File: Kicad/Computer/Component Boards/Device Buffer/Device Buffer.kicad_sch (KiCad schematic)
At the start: 18 parts, among them IC1 SN74ABT245BDBR, IC2 SN74ABT245BDBR, IC3 SN74ABT245BDBR, IC4 SN74ABT245BDBR, IC5 AP7365-33WG-7, J2 Conn_02x32_Counter_Clockwise

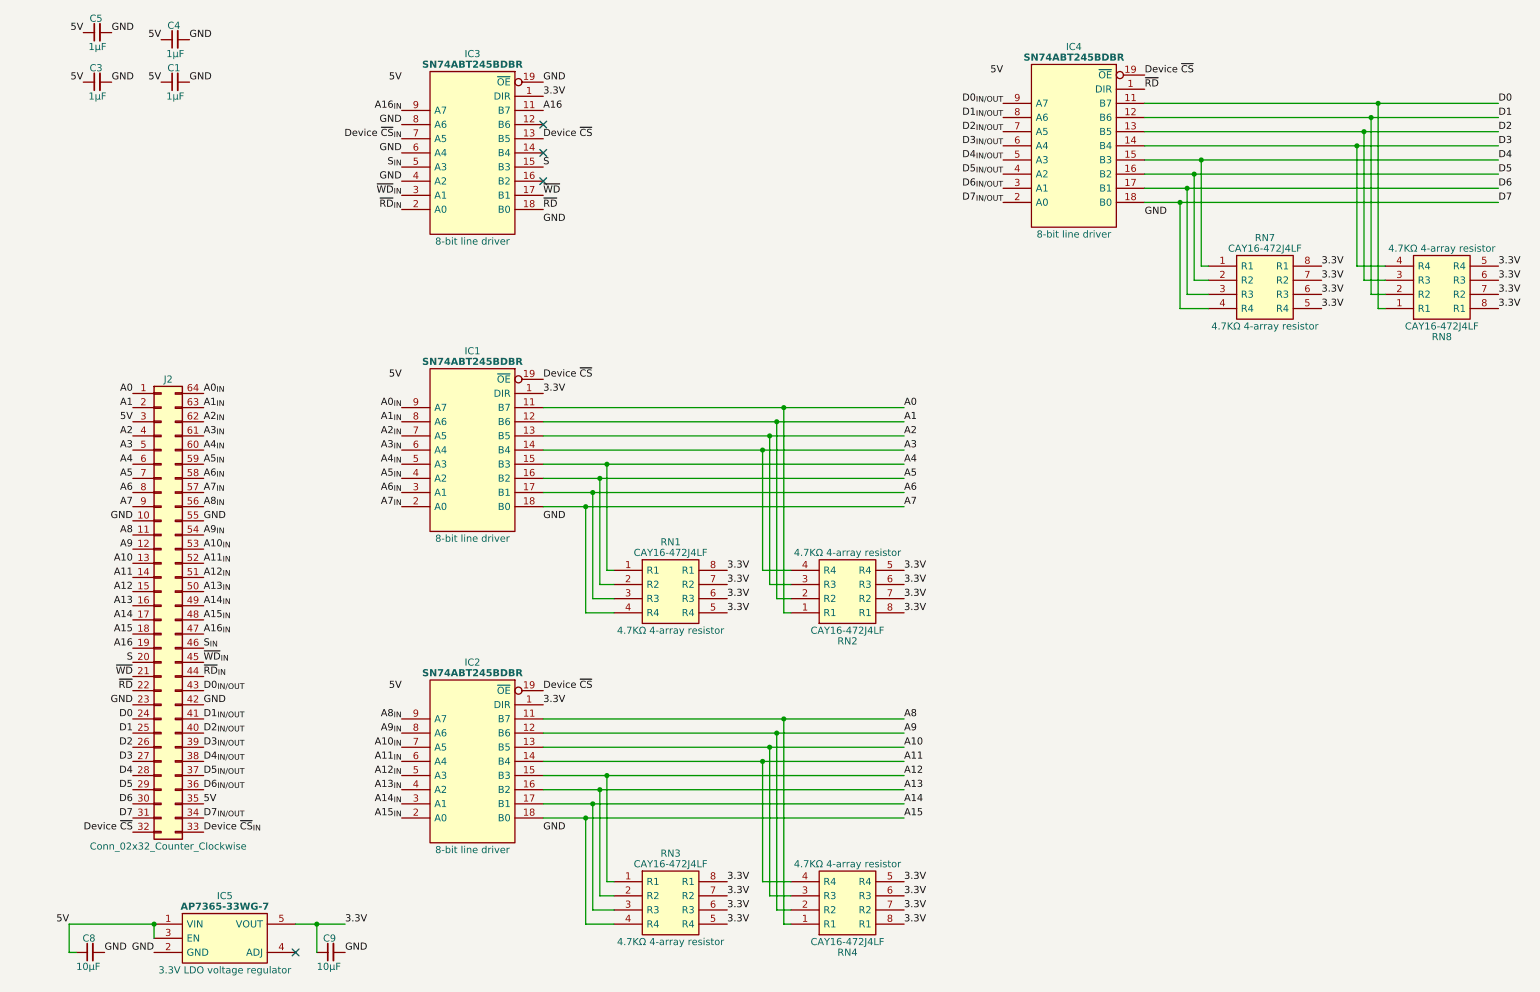
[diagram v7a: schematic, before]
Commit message: Swapped Device Buffer pin sides and re-routed.
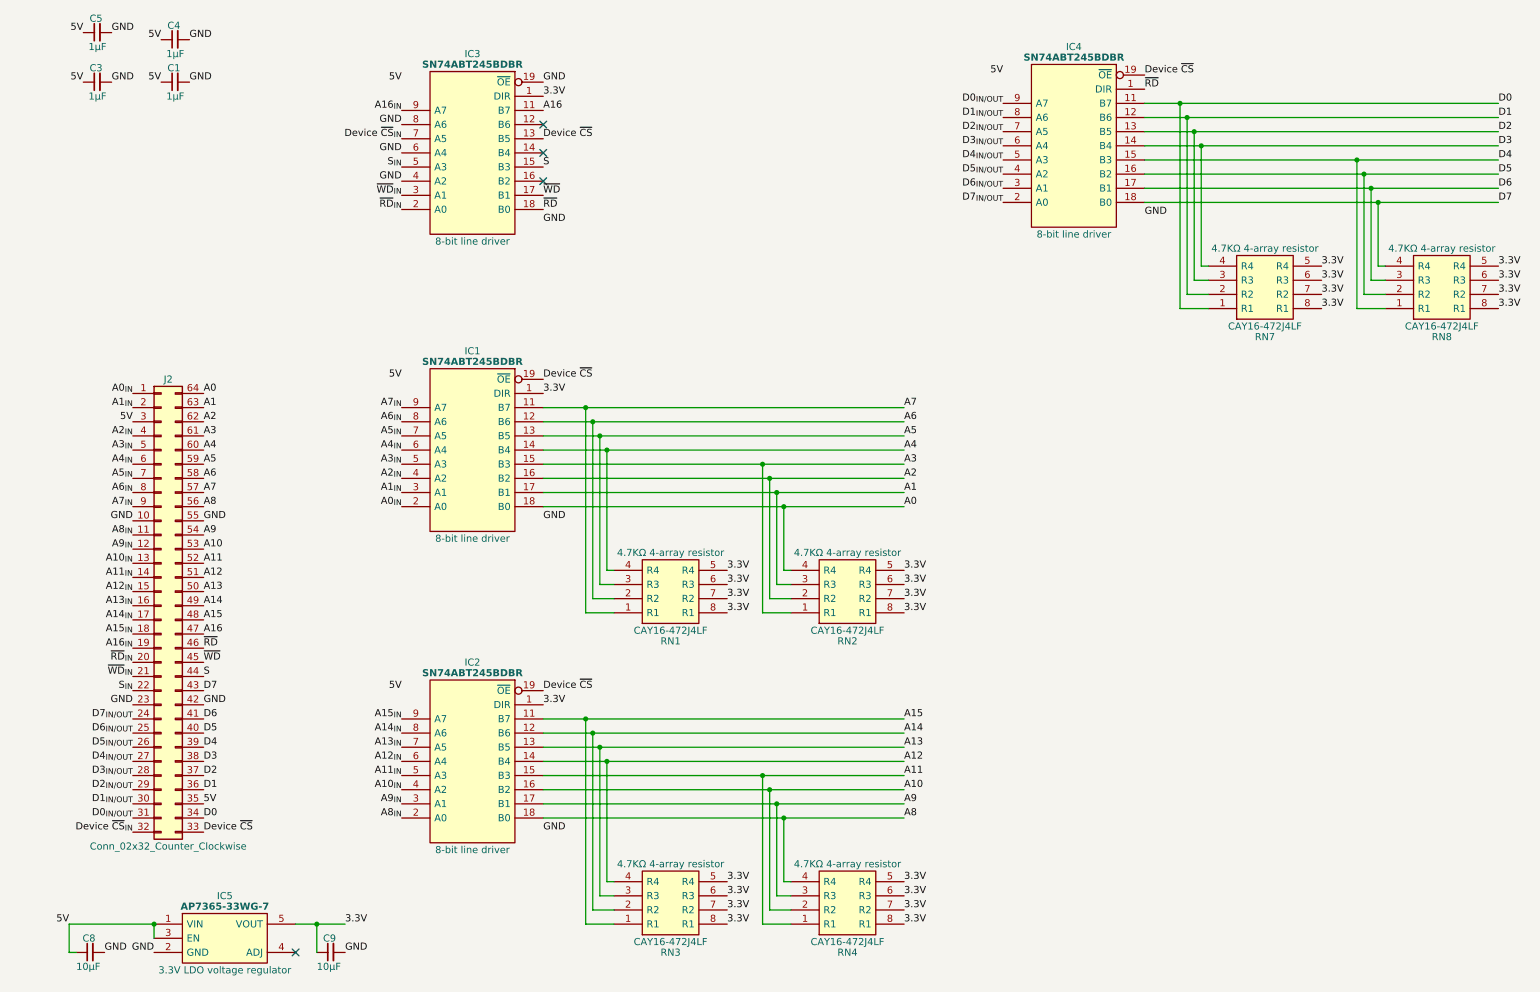
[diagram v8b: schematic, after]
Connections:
- net A0: now also IC1.18 (B0), J2.64 (Pin_64), RN2.4 (R4); no longer IC1.11 (B7), J2.1 (Pin_1), RN2.1 (R1)
- net A0_{IN}: now also IC1.2 (A0), J2.1 (Pin_1); no longer IC1.9 (A7), J2.64 (Pin_64)
- net A1: now also IC1.17 (B1), J2.63 (Pin_63), RN2.3 (R3); no longer IC1.12 (B6), J2.2 (Pin_2), RN2.2 (R2)
- net A10: now also IC2.16 (B2), J2.53 (Pin_53), RN4.2 (R2); no longer IC2.13 (B5), J2.13 (Pin_13), RN4.3 (R3)
- net A10_{IN}: now also IC2.4 (A2), J2.13 (Pin_13); no longer IC2.7 (A5), J2.53 (Pin_53)
- net A11: now also IC2.15 (B3), J2.52 (Pin_52), RN4.1 (R1); no longer IC2.14 (B4), J2.14 (Pin_14), RN4.4 (R4)
- net A11_{IN}: now also IC2.5 (A3), J2.14 (Pin_14); no longer IC2.6 (A4), J2.52 (Pin_52)
- net A12: now also IC2.14 (B4), J2.51 (Pin_51), RN3.4 (R4); no longer IC2.15 (B3), J2.15 (Pin_15), RN3.1 (R1)
- net A12_{IN}: now also IC2.6 (A4), J2.15 (Pin_15); no longer IC2.5 (A3), J2.51 (Pin_51)
- net A13: now also IC2.13 (B5), J2.50 (Pin_50), RN3.3 (R3); no longer IC2.16 (B2), J2.16 (Pin_16), RN3.2 (R2)
- net A13_{IN}: now also IC2.7 (A5), J2.16 (Pin_16); no longer IC2.4 (A2), J2.50 (Pin_50)
- net A14: now also IC2.12 (B6), J2.49 (Pin_49), RN3.2 (R2); no longer IC2.17 (B1), J2.17 (Pin_17), RN3.3 (R3)
- net A14_{IN}: now also IC2.8 (A6), J2.17 (Pin_17); no longer IC2.3 (A1), J2.49 (Pin_49)
- net A15: now also IC2.11 (B7), J2.48 (Pin_48), RN3.1 (R1); no longer IC2.18 (B0), J2.18 (Pin_18), RN3.4 (R4)
- net A15_{IN}: now also IC2.9 (A7), J2.18 (Pin_18); no longer IC2.2 (A0), J2.48 (Pin_48)
- net A16: now also J2.47 (Pin_47); no longer J2.19 (Pin_19)
- net A16_{IN}: now also J2.19 (Pin_19); no longer J2.47 (Pin_47)
- net A1_{IN}: now also IC1.3 (A1), J2.2 (Pin_2); no longer IC1.8 (A6), J2.63 (Pin_63)
- net A2: now also IC1.16 (B2), J2.62 (Pin_62), RN2.2 (R2); no longer IC1.13 (B5), J2.4 (Pin_4), RN2.3 (R3)
- net A2_{IN}: now also IC1.4 (A2), J2.4 (Pin_4); no longer IC1.7 (A5), J2.62 (Pin_62)
- net A3: now also IC1.15 (B3), J2.61 (Pin_61), RN2.1 (R1); no longer IC1.14 (B4), J2.5 (Pin_5), RN2.4 (R4)
- net A3_{IN}: now also IC1.5 (A3), J2.5 (Pin_5); no longer IC1.6 (A4), J2.61 (Pin_61)
- net A4: now also IC1.14 (B4), J2.60 (Pin_60), RN1.4 (R4); no longer IC1.15 (B3), J2.6 (Pin_6), RN1.1 (R1)
- net A4_{IN}: now also IC1.6 (A4), J2.6 (Pin_6); no longer IC1.5 (A3), J2.60 (Pin_60)
- net A5: now also IC1.13 (B5), J2.59 (Pin_59), RN1.3 (R3); no longer IC1.16 (B2), J2.7 (Pin_7), RN1.2 (R2)
- net A5_{IN}: now also IC1.7 (A5), J2.7 (Pin_7); no longer IC1.4 (A2), J2.59 (Pin_59)
- net A6: now also IC1.12 (B6), J2.58 (Pin_58), RN1.2 (R2); no longer IC1.17 (B1), J2.8 (Pin_8), RN1.3 (R3)
- net A6_{IN}: now also IC1.8 (A6), J2.8 (Pin_8); no longer IC1.3 (A1), J2.58 (Pin_58)
- net A7: now also IC1.11 (B7), J2.57 (Pin_57), RN1.1 (R1); no longer IC1.18 (B0), J2.9 (Pin_9), RN1.4 (R4)
- net A7_{IN}: now also IC1.9 (A7), J2.9 (Pin_9); no longer IC1.2 (A0), J2.57 (Pin_57)
- net A8: now also IC2.18 (B0), J2.56 (Pin_56), RN4.4 (R4); no longer IC2.11 (B7), J2.11 (Pin_11), RN4.1 (R1)
- net A8_{IN}: now also IC2.2 (A0), J2.11 (Pin_11); no longer IC2.9 (A7), J2.56 (Pin_56)
- net A9: now also IC2.17 (B1), J2.54 (Pin_54), RN4.3 (R3); no longer IC2.12 (B6), J2.12 (Pin_12), RN4.2 (R2)
- net A9_{IN}: now also IC2.3 (A1), J2.12 (Pin_12); no longer IC2.8 (A6), J2.54 (Pin_54)
- net D0: now also J2.34 (Pin_34), RN7.1 (R1); no longer J2.24 (Pin_24), RN8.1 (R1)
- net D0_{IN/OUT}: now also J2.31 (Pin_31); no longer J2.43 (Pin_43)
- net D1: now also J2.36 (Pin_36), RN7.2 (R2); no longer J2.25 (Pin_25), RN8.2 (R2)
- net D1_{IN/OUT}: now also J2.30 (Pin_30); no longer J2.41 (Pin_41)
- net D2: now also J2.37 (Pin_37), RN7.3 (R3); no longer J2.26 (Pin_26), RN8.3 (R3)
- net D2_{IN/OUT}: now also J2.29 (Pin_29); no longer J2.40 (Pin_40)
- net D3: now also J2.38 (Pin_38), RN7.4 (R4); no longer J2.27 (Pin_27), RN8.4 (R4)
- net D3_{IN/OUT}: now also J2.28 (Pin_28); no longer J2.39 (Pin_39)
- net D4: now also J2.39 (Pin_39), RN8.1 (R1); no longer J2.28 (Pin_28), RN7.1 (R1)
- net D4_{IN/OUT}: now also J2.27 (Pin_27); no longer J2.38 (Pin_38)
- net D5: now also J2.40 (Pin_40), RN8.2 (R2); no longer J2.29 (Pin_29), RN7.2 (R2)
- net D5_{IN/OUT}: now also J2.26 (Pin_26); no longer J2.37 (Pin_37)
- net D6: now also J2.41 (Pin_41), RN8.3 (R3); no longer J2.30 (Pin_30), RN7.3 (R3)
- net D6_{IN/OUT}: now also J2.25 (Pin_25); no longer J2.36 (Pin_36)
- net D7: now also J2.43 (Pin_43), RN8.4 (R4); no longer J2.31 (Pin_31), RN7.4 (R4)
- net D7_{IN/OUT}: now also J2.24 (Pin_24); no longer J2.34 (Pin_34)
- net Device ~{CS}: now also J2.33 (Pin_33); no longer J2.32 (Pin_32)
- net Device ~{CS}_{IN}: now also J2.32 (Pin_32); no longer J2.33 (Pin_33)
- net S: now also J2.44 (Pin_44); no longer J2.20 (Pin_20)
- net S_{IN}: now also J2.22 (Pin_22); no longer J2.46 (Pin_46)
- net ~{RD}: now also J2.46 (Pin_46); no longer J2.22 (Pin_22)
- net ~{RD}_{IN}: now also J2.20 (Pin_20); no longer J2.44 (Pin_44)
- net ~{WD}: now also J2.45 (Pin_45); no longer J2.21 (Pin_21)
- net ~{WD}_{IN}: now also J2.21 (Pin_21); no longer J2.45 (Pin_45)
